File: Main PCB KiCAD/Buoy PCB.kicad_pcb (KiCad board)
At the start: 2 copper layers, 123.5 x 100 mm, 49 parts, among them J1 RS485, J10 USB_B_Micro, J11 Conn_01x12_Socket, J2 Conn_01x12_Socket, J3 Conn_01x12_Pin, J8 Conn_01x12_Pin, J9 Conn_01x12_Socket, Q1 Q_NMOS_DSG, Q2 Q_NMOS_DSG, U3 ESP32-S2-WROVER, U4 MAX3072E

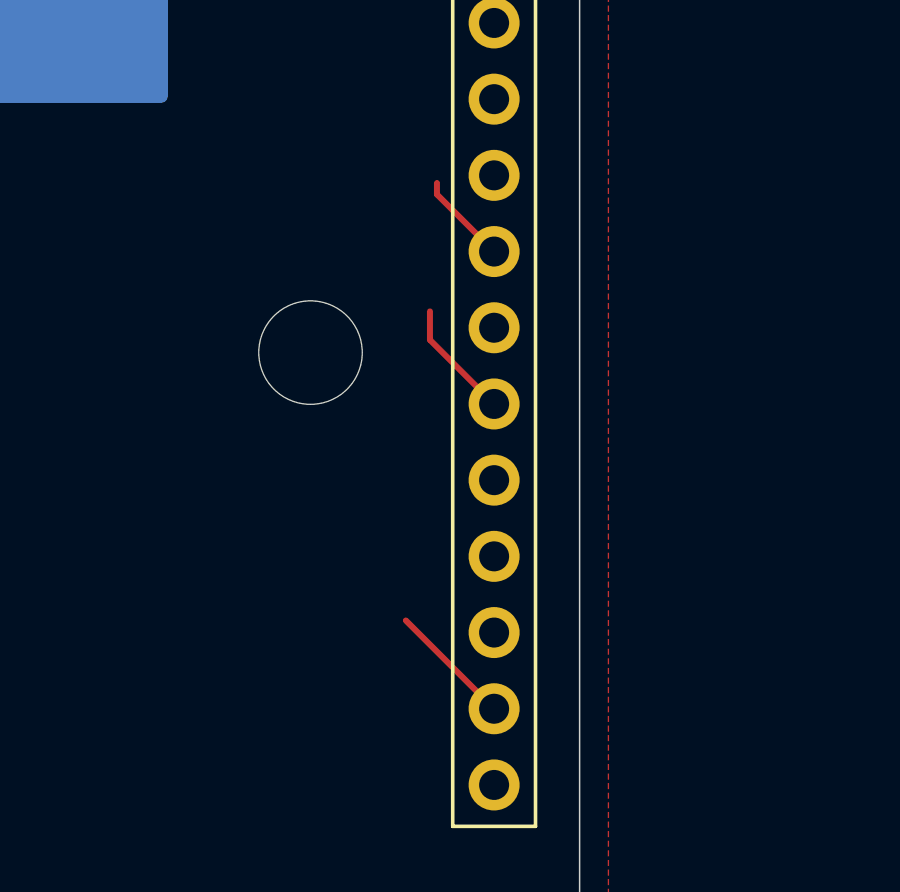
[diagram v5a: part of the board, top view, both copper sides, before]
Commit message: moved connector
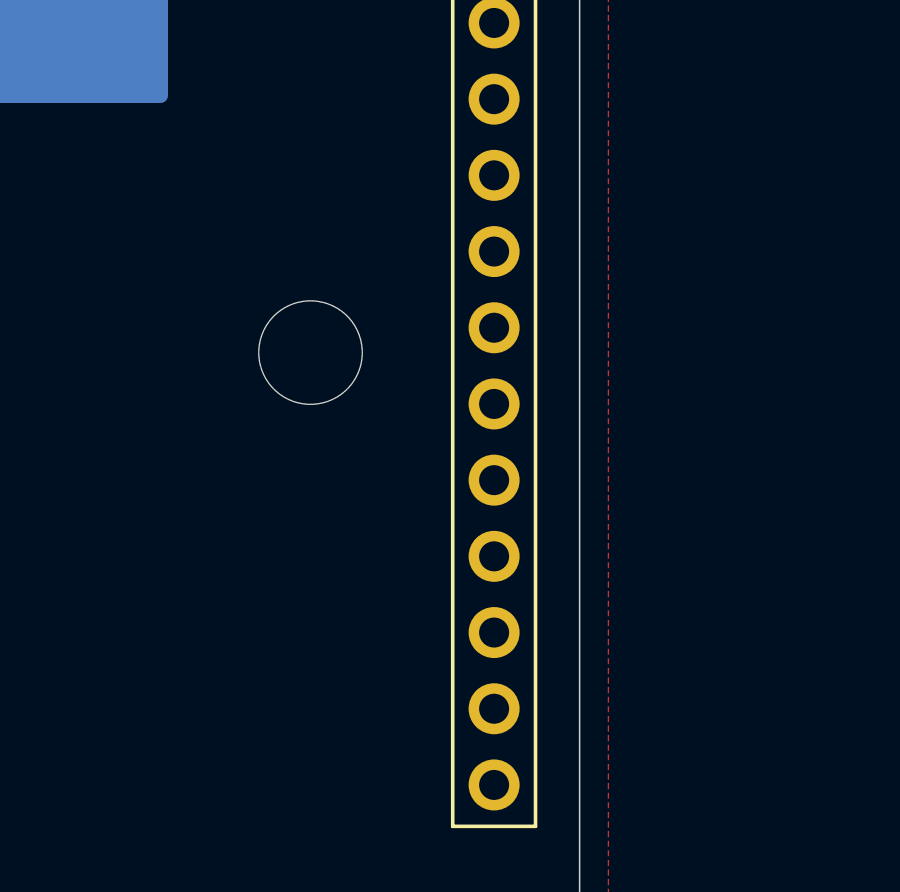
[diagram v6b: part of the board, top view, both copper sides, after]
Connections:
- J2 pad 12: unconnected-(J2-Pin_12-Pad12) -> GND
- J3 pad 12: unconnected-(J3-Pin_12-Pad12) -> GND_Batt
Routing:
- net unconnected-(J3-Pin_11-Pad11): track 4.16 -> 0.00 mm
- net unconnected-(J3-Pin_7-Pad7): track 3.97 -> 0.00 mm
- net unconnected-(J3-Pin_5-Pad5): track 3.07 -> 0.00 mm
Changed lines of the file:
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@@
 	(net 114 "unconnected-(J2-Pin_11-Pad11)")
 	(net 115 "unconnected-(J2-Pin_3-Pad3)")
-	(net 116 "unconnected-(J2-Pin_12-Pad12)")
-	(net 117 "unconnected-(J2-Pin_6-Pad6)")
-	(net 118 "unconnected-(J3-Pin_8-Pad8)")
-	(net 119 "unconnected-(J3-Pin_5-Pad5)")
-	(net 120 "unconnected-(J3-Pin_10-Pad10)")
-	(net 121 "unconnected-(J3-Pin_4-Pad4)")
-	(net 122 "unconnected-(J3-Pin_6-Pad6)")
-	(net 123 "unconnected-(J3-Pin_12-Pad12)")
-	(net 124 "unconnected-(J3-Pin_1-Pad1)")
-	(net 125 "unconnected-(J3-Pin_7-Pad7)")
-	(net 126 "unconnected-(J3-Pin_11-Pad11)")
-	(net 127 "unconnected-(J3-Pin_9-Pad9)")
-	(net 128 "unconnected-(J3-Pin_3-Pad3)")
-	(net 129 "unconnected-(J3-Pin_2-Pad2)")
+	(net 116 "unconnected-(J2-Pin_6-Pad6)")
+	(net 117 "unconnected-(J3-Pin_8-Pad8)")
+	(net 118 "unconnected-(J3-Pin_5-Pad5)")
+	(net 119 "unconnected-(J3-Pin_10-Pad10)")
+	(net 120 "unconnected-(J3-Pin_4-Pad4)")
+	(net 121 "unconnected-(J3-Pin_6-Pad6)")
+	(net 122 "unconnected-(J3-Pin_1-Pad1)")
+	(net 123 "unconnected-(J3-Pin_7-Pad7)")
+	(net 124 "unconnected-(J3-Pin_11-Pad11)")
+	(net 125 "unconnected-(J3-Pin_9-Pad9)")
+	(net 126 "unconnected-(J3-Pin_3-Pad3)")
+	(net 127 "unconnected-(J3-Pin_2-Pad2)")
 	(footprint "Jumper:SolderJumper-2_P1.3mm_Bridged_RoundedPad1.0x1.5mm"
 		(layer "F.Cu")
@@
 			(layers "*.Cu" "*.Mask")
 			(remove_unused_layers no)
-			(net 124 "unconnected-(J3-Pin_1-Pad1)")
+			(net 122 "unconnected-(J3-Pin_1-Pad1)")
 			(pinfunction "Pin_1")
 			(pintype "passive")
@@
 			(layers "*.Cu" "*.Mask")
 			(remove_unused_layers no)
-			(net 129 "unconnected-(J3-Pin_2-Pad2)")
+			(net 127 "unconnected-(J3-Pin_2-Pad2)")
 			(pinfunction "Pin_2")
 			(pintype "passive")
@@
 			(layers "*.Cu" "*.Mask")
 			(remove_unused_layers no)
-			(net 128 "unconnected-(J3-Pin_3-Pad3)")
+			(net 126 "unconnected-(J3-Pin_3-Pad3)")
 			(pinfunction "Pin_3")
 			(pintype "passive")
@@
 			(layers "*.Cu" "*.Mask")
 			(remove_unused_layers no)
-			(net 121 "unconnected-(J3-Pin_4-Pad4)")
+			(net 120 "unconnected-(J3-Pin_4-Pad4)")
 			(pinfunction "Pin_4")
 			(pintype "passive")
@@
 			(layers "*.Cu" "*.Mask")
 			(remove_unused_layers no)
-			(net 119 "unconnected-(J3-Pin_5-Pad5)")
+			(net 118 "unconnected-(J3-Pin_5-Pad5)")
 			(pinfunction "Pin_5")
 			(pintype "passive")
@@
 			(layers "*.Cu" "*.Mask")
 			(remove_unused_layers no)
-			(net 122 "unconnected-(J3-Pin_6-Pad6)")
+			(net 121 "unconnected-(J3-Pin_6-Pad6)")
 			(pinfunction "Pin_6")
 			(pintype "passive")
@@
 			(layers "*.Cu" "*.Mask")
 			(remove_unused_layers no)
-			(net 125 "unconnected-(J3-Pin_7-Pad7)")
+			(net 123 "unconnected-(J3-Pin_7-Pad7)")
 			(pinfunction "Pin_7")
 			(pintype "passive")
@@
 			(layers "*.Cu" "*.Mask")
 			(remove_unused_layers no)
-			(net 118 "unconnected-(J3-Pin_8-Pad8)")
+			(net 117 "unconnected-(J3-Pin_8-Pad8)")
 			(pinfunction "Pin_8")
 			(pintype "passive")
@@
 			(layers "*.Cu" "*.Mask")
 			(remove_unused_layers no)
-			(net 127 "unconnected-(J3-Pin_9-Pad9)")
+			(net 125 "unconnected-(J3-Pin_9-Pad9)")
 			(pinfunction "Pin_9")
 			(pintype "passive")
@@
 			(layers "*.Cu" "*.Mask")
 			(remove_unused_layers no)
-			(net 120 "unconnected-(J3-Pin_10-Pad10)")
+			(net 119 "unconnected-(J3-Pin_10-Pad10)")
 			(pinfunction "Pin_10")
 			(pintype "passive")
@@
 			(layers "*.Cu" "*.Mask")
 			(remove_unused_layers no)
-			(net 126 "unconnected-(J3-Pin_11-Pad11)")
+			(net 124 "unconnected-(J3-Pin_11-Pad11)")
 			(pinfunction "Pin_11")
 			(pintype "passive")
@@
 			(layers "*.Cu" "*.Mask")
 			(remove_unused_layers no)
-			(net 123 "unconnected-(J3-Pin_12-Pad12)")
+			(net 24 "GND_Batt")
 			(pinfunction "Pin_12")
 			(pintype "passive")
@@
 			(layers "*.Cu" "*.Mask")
 			(remove_unused_layers no)
-			(net 117 "unconnected-(J2-Pin_6-Pad6)")
+			(net 116 "unconnected-(J2-Pin_6-Pad6)")
 			(pinfunction "Pin_6")
 			(pintype "passive")
@@
 			(layers "*.Cu" "*.Mask")
 			(remove_unused_layers no)
-			(net 116 "unconnected-(J2-Pin_12-Pad12)")
+			(net 1 "GND")
 			(pinfunction "Pin_12")
 			(pintype "passive")
@@
 		(net 105)
 	)
-	(segment
-		(start 172.72 53.34)
-		(end 170.815 51.435)
-		(width 0.2)
-		(layer "F.Cu")
-		(net 119)
-	)
-	(segment
-		(start 170.815 51.055)
-		(end 170.815 51.435)
-		(width 0.2)
-		(layer "F.Cu")
-		(net 119)
-	)
-	(segment
-		(start 170.581 56.281)
-		(end 172.72 58.42)
-		(width 0.2)
-		(layer "F.Cu")
-		(net 125)
-	)
-	(segment
-		(start 170.581 55.3339)
-		(end 170.581 56.281)
-		(width 0.2)
-		(layer "F.Cu")
-		(net 125)
-	)
-	(segment
-		(start 169.779 65.639)
-		(end 172.72 68.58)
-		(width 0.2)
-		(layer "F.Cu")
-		(net 126)
-	)
 	(zone

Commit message: updates
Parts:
- removed BT1, BT2: 18650, Battery:BatteryHolder_Keystone_1042_1x18650
- removed U3: ESP32-S2-WROVER, RF_Module:ESP32-S2-WROVER
- added C1: 100nF, Capacitor_SMD:C_0805_2012Metric_Pad1.18x1.45mm_HandSolder, F.Cu at (79.5, 91.6)
- added C11: 22pF, Capacitor_SMD:C_0805_2012Metric_Pad1.18x1.45mm_HandSolder, F.Cu at (79.5, 103.6)
- added C2: 10uF, Capacitor_SMD:C_Elec_6.3x5.8, F.Cu at (89.2, 109.2)
- added C3: 100nF, Capacitor_SMD:C_0805_2012Metric_Pad1.18x1.45mm_HandSolder, F.Cu at (79.5, 94.6)
- added C4: 100nF, Capacitor_SMD:C_0805_2012Metric_Pad1.18x1.45mm_HandSolder, F.Cu at (79.5, 97.6)
- added C5: 22pF, Capacitor_SMD:C_0805_2012Metric_Pad1.18x1.45mm_HandSolder, F.Cu at (79.5, 100.6)
- added D8: Green, Diode_SMD:D_0805_2012Metric_Pad1.15x1.40mm_HandSolder, F.Cu at (86.6, 121.8)
- added J12: Conn_01x12_Socket, Connector_PinSocket_2.54mm:PinSocket_1x12_P2.54mm_Vertical, F.Cu at (67.3, 36.8)
- added J13: Conn_01x12_Pin, Connector_PinHeader_2.54mm:PinHeader_1x12_P2.54mm_Vertical, B.Cu at (246.4, 41.9)
- added J4: UART, Connector_PinHeader_2.54mm:PinHeader_1x05_P2.54mm_Vertical, F.Cu at (84.2, 92.4)
- added J5: ICSP, Connector_PinHeader_2.54mm:PinHeader_2x03_P2.54mm_Vertical, F.Cu at (79.3, 107.4)
- added J6: I2C, Connector_PinHeader_2.54mm:PinHeader_1x04_P2.54mm_Vertical, F.Cu at (93.5, 92.4)
- added J7: Cell, Connector_PinSocket_2.54mm:PinSocket_1x02_P2.54mm_Vertical, F.Cu at (168.9, 120.7)
- added R1: 10k, Resistor_SMD:R_0805_2012Metric_Pad1.20x1.40mm_HandSolder, F.Cu at (88.8, 91.5)
- added R2: 10k, Resistor_SMD:R_0805_2012Metric_Pad1.20x1.40mm_HandSolder, F.Cu at (88.8, 94.5)
- added R20: 1M, Resistor_SMD:R_0805_2012Metric_Pad1.20x1.40mm_HandSolder, F.Cu at (88.8, 100.4)
- added R21: 10k, Resistor_SMD:R_0805_2012Metric_Pad1.20x1.40mm_HandSolder, F.Cu at (88.8, 103.3)
- added R3: 1k, Resistor_SMD:R_0805_2012Metric_Pad1.20x1.40mm_HandSolder, F.Cu at (88.8, 97.4)
- added TP1: HB, TestPoint:TestPoint_Pad_D1.0mm, F.Cu at (78.6, 116.3)
- added TP2: 5V, TestPoint:TestPoint_Pad_D1.0mm, F.Cu at (78.6, 119.4)
- added TP3: GND, TestPoint:TestPoint_Pad_D1.0mm, F.Cu at (78.6, 122.4)
- added U1: ATmega328P-P, Package_DIP:DIP-28_W7.62mm, F.Cu at (67.8, 92.1)
- added Y1: 16 MHz, Crystal:Crystal_SMD_EuroQuartz_MQ-4Pin_7.0x5.0mm_HandSoldering, F.Cu at (90.4, 116.8)
- D2: value RED -> Red; footprint LED_SMD:LED_0805_2012Metric_Pad1.15x1.40mm_HandSolder -> Diode_SMD:D_0805_2012Metric_Pad1.15x1.40mm_HandSolder
- R4: value 330 -> 1k
- moved JP4 104.7 mm to (147.3, 47.3)
- moved R15 104.7 mm to (143.5, 47.3)
- moved R17 104.7 mm to (141.0, 47.3)
- moved R6 104.7 mm to (147.3, 56.1)
- moved R5 104.7 mm to (147.3, 52.3)
- moved R18 104.7 mm to (138.4, 47.3)
- moved R8 104.7 mm to (142.2, 52.3)
- moved R9 104.7 mm to (142.2, 56.1)
- moved C6 64.1 mm to (159.0, 67.3)
- moved C7 64.1 mm to (157.7, 78.7)
- moved R14 62.6 mm to (221.0, 58.1), turned to -90 degrees
- moved D15 61.0 mm to (218.4, 58.1), turned to -90 degrees
- moved R13 57.9 mm to (221.0, 54.3), turned to -90 degrees
- moved D14 56.1 mm to (218.4, 54.3), turned to -90 degrees
- moved C8 54.8 mm to (147.6, 85.9)
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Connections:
- R4 pad 1: +3.3V -> Net-(D8-A)
- R4 pad 2: Net-(D2-A) -> +5V
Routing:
- net +Batt: track 7.04 -> 17.3 mm, vias 2 -> 1
- net -Batt: track 9.06 -> 18.3 mm, vias 1 -> 0
- net GND_Batt: track 6.50 -> 5.98 mm
- added copper zone on B.Cu, net GND
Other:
- board size 123.5 x 100 mm -> 219.2 x 111.7 mm

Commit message: update
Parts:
- removed J13: Conn_01x12_Pin, Connector_PinHeader_2.54mm:PinHeader_1x12_P2.54mm_Vertical
- removed JP4: LEDs, Jumper:SolderJumper-2_P1.3mm_Bridged_RoundedPad1.0x1.5mm
- removed JP6: Terminator, Jumper:SolderJumper-2_P1.3mm_Open_RoundedPad1.0x1.5mm
- added D10: 1N5819HW-FDICT, Diode_SMD:D_SOD-123, F.Cu at (234.2, 128.6)
- added D11: RED, LED_SMD:LED_0805_2012Metric_Pad1.15x1.40mm_HandSolder, F.Cu at (233.7, 131.7)
- added D16: WS2812B, LED_SMD:LED_WS2812B_PLCC4_5.0x5.0mm_P3.2mm, F.Cu at (225.8, 36.3)
- added D17: WS2812B, LED_SMD:LED_WS2812B_PLCC4_5.0x5.0mm_P3.2mm, F.Cu at (239.8, 77.5)
- added JP2: RS485 - Power, Jumper:SolderJumper-2_P1.3mm_Bridged_RoundedPad1.0x1.5mm, F.Cu at (233.5, 123.1)
- added JP3: LEDs, Jumper:SolderJumper-2_P1.3mm_Bridged_RoundedPad1.0x1.5mm, F.Cu at (238.3, 132.0)
- added U2: MAX3072E, Package_SO:SOIC-8_3.9x4.9mm_P1.27mm, F.Cu at (235.5, 118.1)
- C10: value 100nF -> 1uF
- C11: value 22pF -> 100nF
- C6: value 1u -> 22pF
- C7: value 1uF -> 1u
- D1: value 1N5819HW-FDICT -> Red; footprint Diode_SMD:D_SOD-123 -> Diode_SMD:D_0805_2012Metric_Pad1.15x1.40mm_HandSolder
- D12, D3: value 1N5819HW-FDICT -> RED; footprint Diode_SMD:D_SOD-123 -> LED_SMD:LED_0805_2012Metric_Pad1.15x1.40mm_HandSolder
- D14, D15: value RED -> WS2812B; footprint LED_SMD:LED_0805_2012Metric_Pad1.15x1.40mm_HandSolder -> LED_SMD:LED_WS2812B_PLCC4_5.0x5.0mm_P3.2mm
- D2: value Red -> Green
- D8: value Green -> 1N5819HW-FDICT; footprint Diode_SMD:D_0805_2012Metric_Pad1.15x1.40mm_HandSolder -> Diode_SMD:D_SOD-123
- D9: value RED -> 1N5819HW-FDICT; footprint LED_SMD:LED_0805_2012Metric_Pad1.15x1.40mm_HandSolder -> Diode_SMD:D_SOD-123
- J1: value RS485 -> Conn_01x12_Socket; footprint Connector_Molex:Molex_Nano-Fit_105309-xx08_1x08_P2.50mm_Vertical -> Connector_PinSocket_2.54mm:PinSocket_1x12_P2.54mm_Vertical
- J11: value Conn_01x12_Socket -> Battery 1; footprint Connector_PinSocket_2.54mm:PinSocket_1x12_P2.54mm_Vertical -> Connector_JST:JST_PH_S2B-PH-K_1x02_P2.00mm_Horizontal
- J12: value Conn_01x12_Socket -> Battery 2; footprint Connector_PinSocket_2.54mm:PinSocket_1x12_P2.54mm_Vertical -> Connector_JST:JST_PH_S2B-PH-K_1x02_P2.00mm_Horizontal
- J4: value UART -> Conn_01x12_Pin; footprint Connector_PinHeader_2.54mm:PinHeader_1x05_P2.54mm_Vertical -> Connector_PinHeader_2.54mm:PinHeader_1x12_P2.54mm_Vertical
- J5: value ICSP -> UART; footprint Connector_PinHeader_2.54mm:PinHeader_2x03_P2.54mm_Vertical -> Connector_PinHeader_2.54mm:PinHeader_1x05_P2.54mm_Vertical
- J6: value I2C -> ICSP; footprint Connector_PinHeader_2.54mm:PinHeader_1x04_P2.54mm_Vertical -> Connector_PinHeader_2.54mm:PinHeader_2x03_P2.54mm_Vertical
- J7: value Cell -> I2C; footprint Connector_PinSocket_2.54mm:PinSocket_1x02_P2.54mm_Vertical -> Connector_PinHeader_2.54mm:PinHeader_1x04_P2.54mm_Vertical
- J8: value Conn_01x12_Pin -> RS485; footprint Connector_PinHeader_2.54mm:PinHeader_1x12_P2.54mm_Vertical -> Connector_Molex:Molex_Nano-Fit_105309-xx08_1x08_P2.50mm_Vertical
- JP1: value RS485 - Power -> Terminator; footprint Jumper:SolderJumper-2_P1.3mm_Bridged_RoundedPad1.0x1.5mm -> Jumper:SolderJumper-2_P1.3mm_Open_RoundedPad1.0x1.5mm
- R10: value 120 -> 1k
- R11: value 1k -> 10k
- R12: value 330 -> 10k
- R13: value 330 -> 1k
- R15: value 22k -> 330
- R19: value 2.7k -> 22k
- R20: value 1M -> 330
- R21: value 10k -> 2.7k
- R5: value 10k -> 1M
- R7: value 1k -> 120
- U4: value MAX3072E -> MCP73834T-FCI/UN
- moved J12 98.1 mm to (164.6, 49.2), turned to 180 degrees
- moved D14 46.9 mm to (265.4, 54.6)
- moved D15 37.2 mm to (240.7, 28.4)
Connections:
- C10 pad 1: Net-(U7-VDD) -> +Batt
- C11 pad 1: Net-(U1-XTAL2/PB7) -> Net-(U5-VDD)
- C11 pad 2: GND -> -Batt
- C6 pad 1: +Solar_Batt -> Net-(U1-XTAL2/PB7)
- C6 pad 2: GND_Batt -> GND
- C7 pad 1: +Batt -> +Solar_Batt
- C7 pad 2: -Batt -> GND_Batt
- D1 pad 1: +Solar_Batt -> GND
- D12 pad 1: +Solar -> Net-(D12-K)
- D12 pad 2: Net-(D12-A) -> Net-(D11-A)
- D13 pad 2: Net-(D13-A) -> Net-(D11-A)
- D14 pad 1: Net-(D14-K) -> +5V
- D14 pad 2: Net-(D13-A) -> Net-(D14-DOUT)
- D15 pad 1: Net-(D15-K) -> +5V
- D15 pad 2: Net-(D13-A) -> Net-(D15-DOUT)
- D3 pad 1: +Solar_Batt -> GND_Batt
- D8 pad 1: GND -> +Solar_Batt
- D9 pad 1: GND_Batt -> +Solar_Batt
- J1 pad 1: Net-(J1-Pin_1) -> +3.3V
- J1 pad 2: /RS485 Interface/Data_A -> +Solar
- J1 pad 3: /RS485 Interface/Data_B -> GND
- J1 pad 5: Net-(J1-Pin_1) -> unconnected-(J1-Pin_5-Pad5)
- J1 pad 6: /RS485 Interface/Data_A -> unconnected-(J1-Pin_6-Pad6)
- J1 pad 7: /RS485 Interface/Data_B -> GND
- J1 pad 8: GND -> unconnected-(J1-Pin_8-Pad8)
- J10 pad 1: Net-(D12-A) -> Net-(D10-A)
- J11 pad 1: Net-(D1-A) -> +Batt
- J11 pad 2: GND_Batt -> -Batt
- J12 pad 1: unconnected-(J12-Pin_1-Pad1) -> +Batt
- J12 pad 2: unconnected-(J12-Pin_2-Pad2) -> -Batt
- J3 pad 1: unconnected-(J3-Pin_1-Pad1) -> +3.3V_bat
- J3 pad 12: GND_Batt -> unconnected-(J3-Pin_12-Pad12)
- J3 pad 2: unconnected-(J3-Pin_2-Pad2) -> +Solar_Batt
- J3 pad 3: unconnected-(J3-Pin_3-Pad3) -> GND_Batt
- J3 pad 4: unconnected-(J3-Pin_4-Pad4) -> GND_Batt
- J3 pad 5: unconnected-(J3-Pin_5-Pad5) -> /V_Batt_An
- J3 pad 6: unconnected-(J3-Pin_6-Pad6) -> /V_Solar_An
- J3 pad 7: unconnected-(J3-Pin_7-Pad7) -> GND_Batt
- J4 pad 1: +5V -> unconnected-(J4-Pin_1-Pad1)
- J4 pad 2: GND -> unconnected-(J4-Pin_2-Pad2)
- J4 pad 3: /Squid/Reset -> unconnected-(J4-Pin_3-Pad3)
- J4 pad 4: /Squid/RX -> unconnected-(J4-Pin_4-Pad4)
- J4 pad 5: /Squid/TX -> unconnected-(J4-Pin_5-Pad5)
- J5 pad 1: /Squid/MISO -> +5V
- J5 pad 2: +5V -> GND
- J5 pad 3: /Squid/SCK -> /Squid/Reset
- J5 pad 4: /Squid/MOSI -> /Squid/RX
- J5 pad 5: /Squid/Reset -> /Squid/TX
- J6 pad 1: +5V -> /Squid/MISO
- J6 pad 2: GND -> +5V
- J6 pad 3: /Squid/SCL -> /Squid/SCK
- J6 pad 4: /Squid/SDA -> /Squid/MOSI
- J7 pad 1: +Batt -> +5V
- J7 pad 2: -Batt -> GND
- J8 pad 1: +3.3V_bat -> Net-(J8-Pin_1)
- J8 pad 2: +Solar_Batt -> /RS485 Interface/Data_A
- J8 pad 3: GND_Batt -> /RS485 Interface/Data_B
- J8 pad 4: GND_Batt -> GND
- J8 pad 5: /V_Batt_An -> Net-(J8-Pin_1)
- J8 pad 6: /V_Solar_An -> /RS485 Interface/Data_A
- J8 pad 7: GND_Batt -> /RS485 Interface/Data_B
- J8 pad 8: unconnected-(J8-Pin_8-Pad8) -> GND
- J9 pad 1: +3.3V -> Net-(D4-A)
- J9 pad 10: unconnected-(J9-Pin_10-Pad10) -> GND_Batt
- J9 pad 11: unconnected-(J9-Pin_11-Pad11) -> Net-(D9-A)
- J9 pad 12: unconnected-(J9-Pin_12-Pad12) -> GND_Batt
- J9 pad 2: +Solar -> GND_Batt
- J9 pad 3: GND -> Net-(D5-A)
- J9 pad 4: GND -> GND_Batt
- J9 pad 5: unconnected-(J9-Pin_5-Pad5) -> Net-(D6-A)
- J9 pad 6: unconnected-(J9-Pin_6-Pad6) -> GND_Batt
- J9 pad 7: GND -> Net-(D7-A)
- J9 pad 8: unconnected-(J9-Pin_8-Pad8) -> GND_Batt
- J9 pad 9: unconnected-(J9-Pin_9-Pad9) -> Net-(D8-A)
- JP1 pad 1: Net-(J1-Pin_1) -> /RS485 Interface/Data_B
- JP1 pad 2: +5V -> Net-(JP1-B)
- R10 pad 1: /RS485 Interface/Data_A -> +Solar_Batt
- R10 pad 2: Net-(JP6-B) -> Net-(D3-A)
- R11 pad 1: Net-(U6-PROG) -> +Batt
- R11 pad 2: GND -> /V_Batt_An
- R12 pad 1: Net-(D13-K) -> /V_Batt_An
- R12 pad 2: /Battery Charger/Status1 -> -Batt
- R13 pad 1: Net-(D14-K) -> Net-(U4-PROG)
- R13 pad 2: /Battery Charger/Status2 -> GND
- R14 pad 1: Net-(D15-K) -> Net-(D11-K)
- R14 pad 2: /Battery Charger/PG -> /Battery Charger/Status1
- R15 pad 1: +3.3V_bat -> Net-(D12-K)
- R15 pad 2: /Battery Charger/Status1 -> /Battery Charger/Status2
- R16 pad 1: +Batt -> Net-(D13-K)
- R16 pad 2: Net-(U7-VDD) -> /Battery Charger/PG
- R17 pad 2: /Battery Charger/Status2 -> /Battery Charger/Status1
- R18 pad 2: /Battery Charger/PG -> /Battery Charger/Status2
- R19 pad 1: Net-(U7-VM) -> +3.3V_bat
- R19 pad 2: GND_Batt -> /Battery Charger/PG
- R20 pad 1: Net-(U1-XTAL2/PB7) -> +Batt
- R20 pad 2: Net-(U1-XTAL1/PB6) -> Net-(U5-VDD)
- R21 pad 1: Net-(U1-~{RESET}/PC6) -> Net-(U5-VM)
- R21 pad 2: +5V -> GND_Batt
- R3 pad 1: Net-(D2-A) -> Net-(D1-A)
- R4 pad 1: Net-(D8-A) -> Net-(D2-A)
- R5 pad 1: +Batt -> Net-(U1-XTAL2/PB7)
- R5 pad 2: /V_Batt_An -> Net-(U1-XTAL1/PB6)
- R6 pad 1: /V_Batt_An -> Net-(U1-~{RESET}/PC6)
- R6 pad 2: -Batt -> +5V
- R7 pad 1: +Solar_Batt -> /RS485 Interface/Data_A
- R7 pad 2: Net-(D9-A) -> Net-(JP1-B)
- U4 pad 1: /RS485 Interface/232_RX -> +Solar_Batt
- U4 pad 2: /RS485 Interface/DIR -> +Solar_Batt
- U4 pad 3: /RS485 Interface/DIR -> /Battery Charger/Status1
- U4 pad 4: /RS485 Interface/232_TX -> /Battery Charger/Status2
- U4 pad 6: /RS485 Interface/Data_A -> Net-(U4-PROG)
- U4 pad 7: /RS485 Interface/Data_B -> /Battery Charger/PG
- U4 pad 8: +5V -> Net-(U4-THERM)
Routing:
- net Net-(D13-A): track 11.4 -> 0.00 mm
- net Net-(D11-A): track 0.00 -> 9.89 mm
- net (no net): track 0.00 -> 8.03 mm
- net Net-(U1-XTAL2/PB7): track 0.00 -> 4.01 mm, vias 0 -> 1
- net +Batt: track 17.3 -> 13.3 mm, vias 1 -> 0
- net Net-(D12-A): track 3.94 -> 0.00 mm
- net Net-(U7-VDD): track 2.56 -> 0.00 mm
- net Net-(U4-PROG): track 0.00 -> 2.55 mm
- net Net-(D14-K): track 2.55 -> 0.00 mm
- net Net-(JP1-B): track 0.00 -> 2.55 mm
- net Net-(D9-A): track 2.55 -> 0.00 mm
- net Net-(D15-K): track 2.55 -> 0.00 mm
- net Net-(D11-K): track 0.00 -> 2.55 mm
